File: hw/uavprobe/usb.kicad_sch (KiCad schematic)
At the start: 45 parts, among them J1 USB_C_Receptacle_USB2.0_14P, SW2 Reset, U6 NCP1117-5.0_SOT223, U7 TPS2561, U8 USB2412-DZK, Y2 24MHz

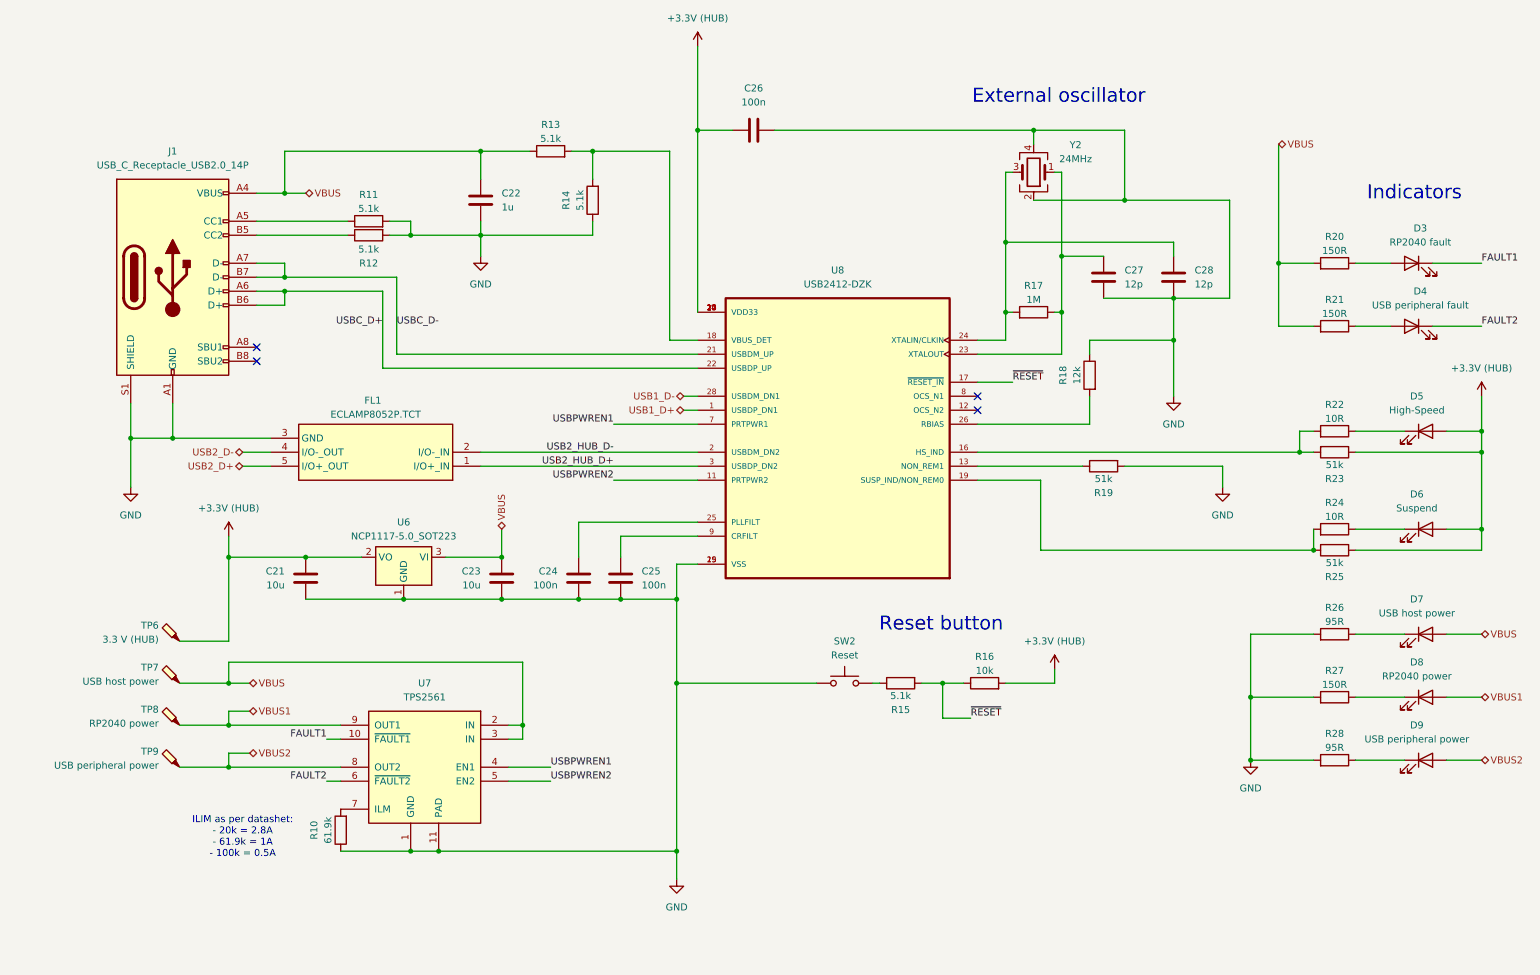
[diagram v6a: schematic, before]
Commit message: Training layout
Lessons were learned, let's restart.
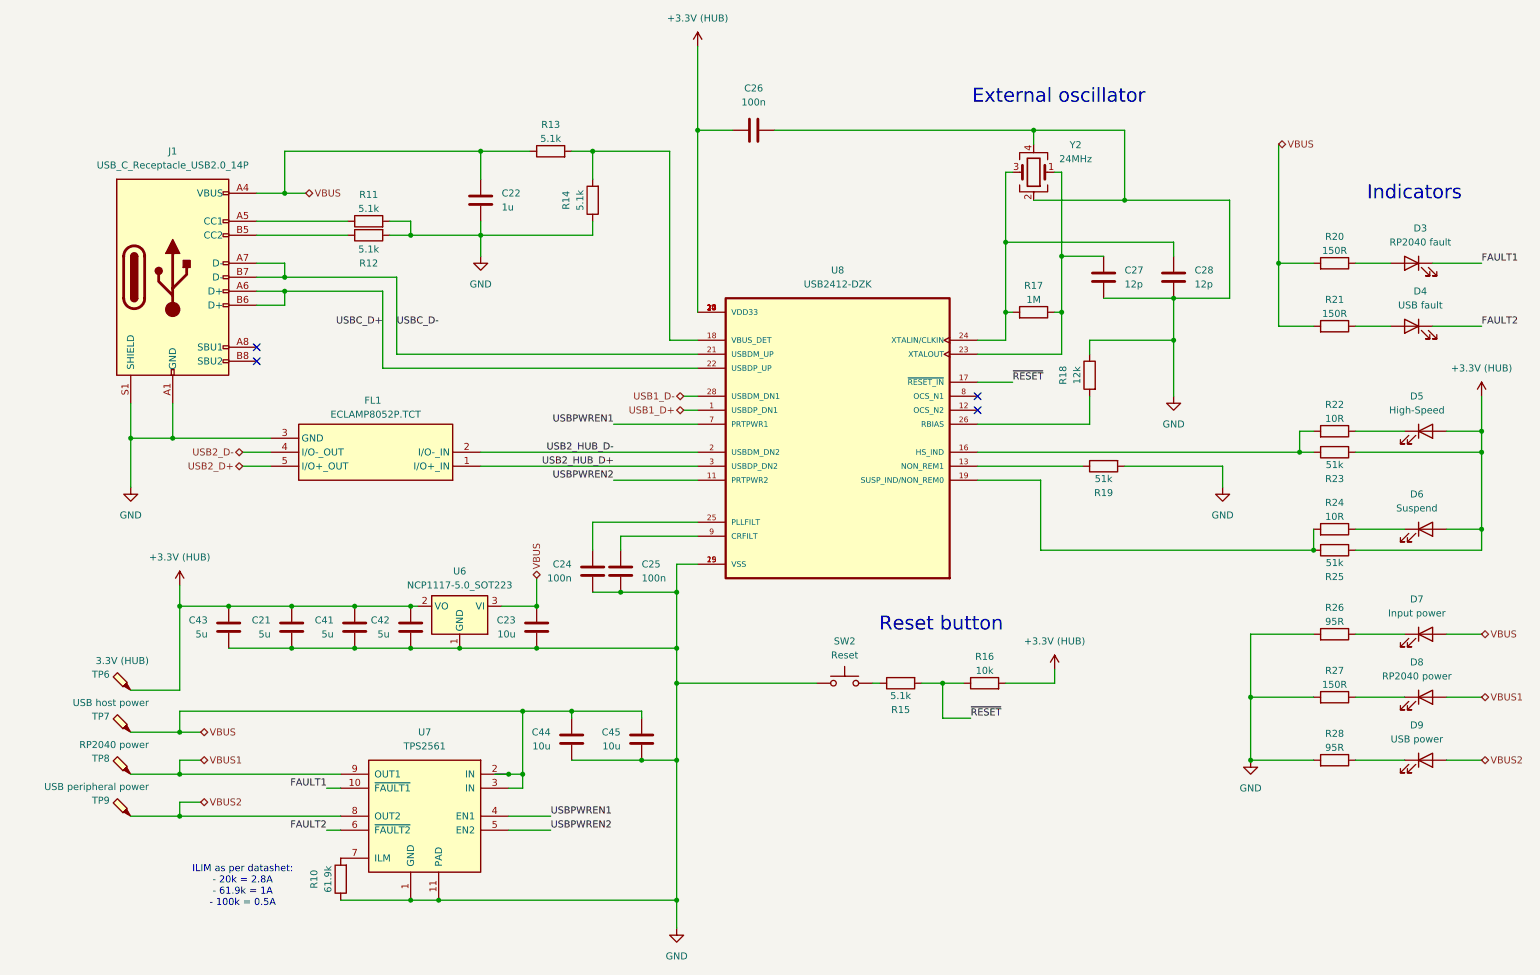
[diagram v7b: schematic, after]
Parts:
- added C41, C42, C43: 5u, Capacitor_SMD:C_0402_1005Metric, symbol Device:C
- added C44, C45: 10u, Capacitor_SMD:C_0402_1005Metric, symbol Device:C
- C21: value 10u -> 5u
- D4: value USB peripheral fault -> USB fault
- D7: value USB host power -> Input power
- D9: value USB peripheral power -> USB power
- R19: footprint Resistor_SMD:R_0402_1005Metric -> Resistor_SMD:R_0603_1608Metric
- TP6: value 3.3 V (HUB) -> 3.3V (HUB)
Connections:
- net +3.3V (HUB): now also C41.1, C42.1, C43.1
- net GND: now also C41.2, C42.2, C43.2, C44.2, C45.2
- net VBUS: now also C44.1, C45.1
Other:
- moved on the sheet: C21, C23, C24, C25, R10, TP6, TP7, TP8, TP9, U6, U7

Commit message: Layout revision 1
Pre-DRC
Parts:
- D3: value RP2040 fault -> MCU fault
- D8: value RP2040 power -> MCU power
- R19: footprint Resistor_SMD:R_0603_1608Metric -> Resistor_SMD:R_0402_1005Metric
- TP6: value 3.3V (HUB) -> 3.3V HUB
- TP7: value USB host power -> 5V USB in
- TP8: value RP2040 power -> 5V USB1
- TP9: value USB peripheral power -> 5V USB2
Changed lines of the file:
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@@
 			)
 		)
-		(property "Value" "RP2040 fault"
+		(property "Value" "MCU fault"
 			(at 264.4775 64.77 0)
 			(effects
@@
 			)
 		)
-		(property "Value" "RP2040 power"
-			(at 33.782 155.956 0)
+		(property "Value" "5V USB1"
+			(at 28.702 155.702 0)
 			(effects
 				(font
@@
 			)
 		)
-		(property "Value" "USB peripheral power"
-			(at 33.782 163.576 0)
+		(property "Value" "5V USB2"
+			(at 28.702 163.83 0)
 			(effects
 				(font
@@
 			)
 		)
-		(property "Footprint" "Resistor_SMD:R_0603_1608Metric"
+		(property "Footprint" "Resistor_SMD:R_0402_1005Metric"
 			(at 207.01 103.632 90)
 			(effects
@@
 			)
 		)
-		(property "Value" "RP2040 power"
+		(property "Value" "MCU power"
 			(at 263.8425 143.51 0)
 			(effects
@@
 			)
 		)
-		(property "Value" "USB host power"
-			(at 33.782 148.336 0)
+		(property "Value" "5V USB in"
+			(at 30.226 148.59 0)
 			(effects
 				(font
@@
 			)
 		)
-		(property "Value" "3.3V (HUB)"
-			(at 33.782 140.716 0)
+		(property "Value" "3.3V HUB"
+			(at 29.972 140.716 0)
 			(effects
 				(font
